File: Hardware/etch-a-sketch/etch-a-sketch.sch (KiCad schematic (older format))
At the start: 37 parts, among them J1 USART, J2 Conn_02x05_Odd_Even, J3 OLED, J4 Micro USB B, SW1 Encoder 1, SW2 Encoder 2, U1 AMS1117-3.3, U2 STM32F401RET6

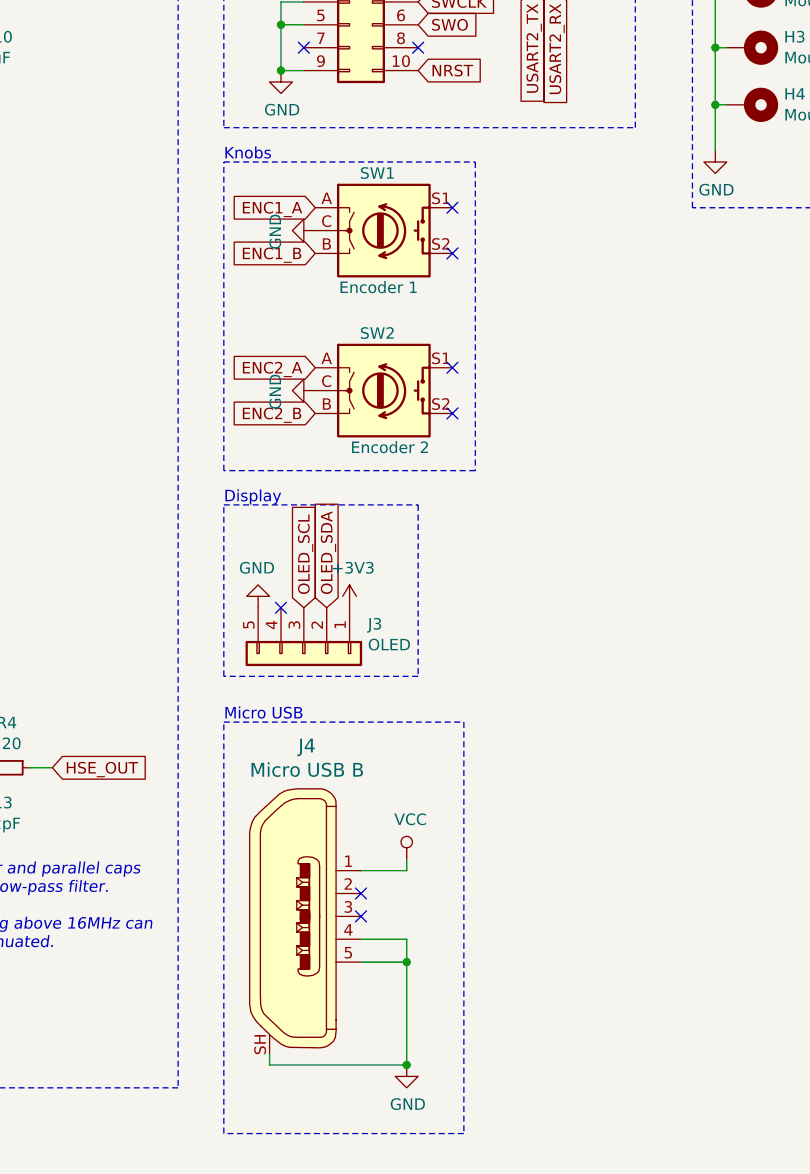
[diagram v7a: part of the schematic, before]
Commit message: feat: connect encoder switches to act as NRST button
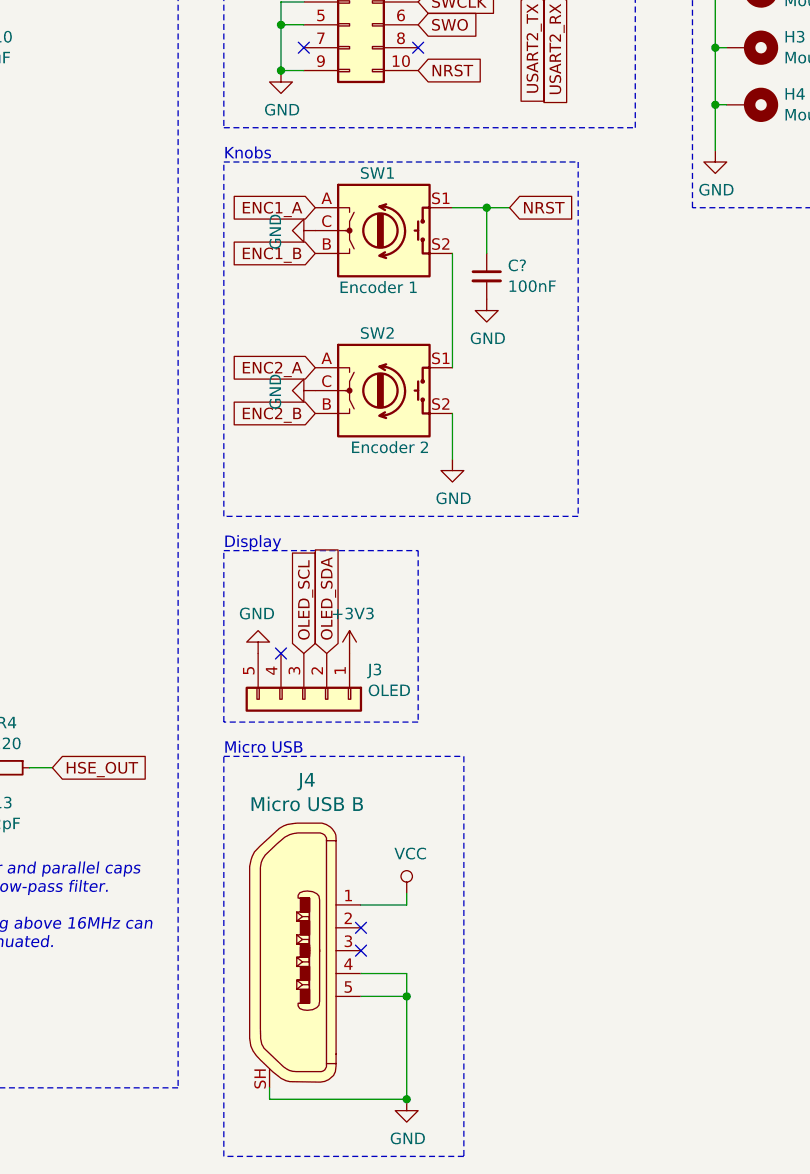
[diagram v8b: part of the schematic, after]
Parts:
- added C?: 100nF, symbol Device:C_Small
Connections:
- net GND: now also SW2.S2, C?.2
- net NRST: now also SW1.S1, C?.1
- net at SW2.S1: now also SW1.S2
- no-connect marks 44 -> 40
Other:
- moved on the sheet: J3, J4
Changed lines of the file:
@@
 NoConn ~ 2850 4300
 NoConn ~ 2850 4200
-NoConn ~ 6400 4450
-NoConn ~ 6400 4250
-NoConn ~ 6400 3750
-NoConn ~ 6400 3550
 $Comp
 L power:GND #PWR013
@@
 L power:GND #PWR019
 U 1 1 5EC0AEF0
-P 5550 5300
-F 0 "#PWR019" H 5550 5050 50  0001 C CNN
-F 1 "GND" H 5555 5127 50  0000 C CNN
-F 2 "" H 5550 5300 50  0001 C CNN
-F 3 "" H 5550 5300 50  0001 C CNN
-	1    5550 5300
+P 5550 5500
+F 0 "#PWR019" H 5550 5250 50  0001 C CNN
+F 1 "GND" H 5555 5327 50  0000 C CNN
+F 2 "" H 5550 5500 50  0001 C CNN
+F 3 "" H 5550 5500 50  0001 C CNN
+	1    5550 5500
 	-1   0    0    1
 $EndComp
-NoConn ~ 5650 5300
-Text GLabel 5850 5300 1    50   Input ~ 0
+NoConn ~ 5650 5500
+Text GLabel 5850 5500 1    50   Input ~ 0
 OLED_SDA
-Text GLabel 5750 5300 1    50   Input ~ 0
+Text GLabel 5750 5500 1    50   Input ~ 0
 OLED_SCL
 $Comp
 L power:+3V3 #PWR020
 U 1 1 5EC0F37C
-P 5950 5300
-F 0 "#PWR020" H 5950 5150 50  0001 C CNN
-F 1 "+3V3" H 5965 5473 50  0000 C CNN
-F 2 "" H 5950 5300 50  0001 C CNN
-F 3 "" H 5950 5300 50  0001 C CNN
-	1    5950 5300
+P 5950 5500
+F 0 "#PWR020" H 5950 5350 50  0001 C CNN
+F 1 "+3V3" H 5965 5673 50  0000 C CNN
+F 2 "" H 5950 5500 50  0001 C CNN
+F 3 "" H 5950 5500 50  0001 C CNN
+	1    5950 5500
 	1    0    0    -1
 $EndComp
@@
 Debug
 Wire Notes Line
-	5400 3350 6500 3350
-Wire Notes Line
-	6500 3350 6500 4700
-Wire Notes Line
-	6500 4700 5400 4700
-Wire Notes Line
-	5400 4700 5400 3350
-Wire Notes Line
-	5400 4850 6250 4850
-Wire Notes Line
-	6250 4850 6250 5600
-Wire Notes Line
-	6250 5600 5400 5600
-Wire Notes Line
-	5400 5600 5400 4850
-Text Notes 5400 4850 0    50   ~ 0
+	5400 3350 6950 3350
+Wire Notes Line
+	6950 3350 6950 4900
+Wire Notes Line
+	6950 4900 5400 4900
+Wire Notes Line
+	5400 4900 5400 3350
+Wire Notes Line
+	5400 5050 6250 5050
+Wire Notes Line
+	6250 5050 6250 5800
+Wire Notes Line
+	6250 5800 5400 5800
+Wire Notes Line
+	5400 5800 5400 5050
+Text Notes 5400 5050 0    50   ~ 0
 Display
 Text Notes 5400 3350 0    50   ~ 0
@@
 L Connector_Generic:Conn_01x05 J3
 U 1 1 5ED42D60
-P 5750 5500
-F 0 "J3" V 5622 5780 50  0000 L CNN
-F 1 "OLED" V 5713 5780 50  0000 L CNN
-F 2 "Connector_PinSocket_2.54mm:PinSocket_1x05_P2.54mm_Vertical" H 5750 5500 50  0001 C CNN
-F 3 "~" H 5750 5500 50  0001 C CNN
-	1    5750 5500
+P 5750 5700
+F 0 "J3" V 5622 5980 50  0000 L CNN
+F 1 "OLED" V 5713 5980 50  0000 L CNN
+F 2 "Connector_PinSocket_2.54mm:PinSocket_1x05_P2.54mm_Vertical" H 5750 5700 50  0001 C CNN
+F 3 "~" H 5750 5700 50  0001 C CNN
+	1    5750 5700
 	0    1    1    0
 $EndComp
@@
 Mounting Holes
 Wire Notes Line
-	5400 5800 6450 5800
-Wire Notes Line
-	6450 5800 6450 7600
-Wire Notes Line
-	6450 7600 5400 7600
-Wire Notes Line
-	5400 7600 5400 5800
-Text Notes 5400 5800 0    50   ~ 0
+	5400 5950 6450 5950
+Wire Notes Line
+	6450 5950 6450 7700
+Wire Notes Line
+	6450 7700 5400 7700
+Wire Notes Line
+	5400 7700 5400 5950
+Text Notes 5400 5950 0    50   ~ 0
 Micro USB
 NoConn ~ 1550 6000
@@
 L dk_USB-DVI-HDMI-Connectors:10118194-0001LF J4
 U 1 1 5EACED3E
-P 5700 6650
-F 0 "J4" H 5764 7395 60  0000 C CNN
-F 1 "Micro USB B" H 5764 7289 60  0000 C CNN
-F 2 "digikey-footprints:USB_Micro_B_Female_10118194-0001LF" H 5900 6850 60  0001 L CNN
-F 3 "http://www.amphenol-icc.com/media/wysiwyg/files/drawing/10118194.pdf" H 5900 6950 60  0001 L CNN
-F 4 "609-4618-1-ND" H 5900 7050 60  0001 L CNN "Digi-Key_PN"
-F 5 "10118194-0001LF" H 5900 7150 60  0001 L CNN "MPN"
-F 6 "Connectors, Interconnects" H 5900 7250 60  0001 L CNN "Category"
-F 7 "USB, DVI, HDMI Connectors" H 5900 7350 60  0001 L CNN "Family"
-F 8 "http://www.amphenol-icc.com/media/wysiwyg/files/drawing/10118194.pdf" H 5900 7450 60  0001 L CNN "DK_Datasheet_Link"
-F 9 "/product-detail/en/amphenol-icc-fci/10118194-0001LF/609-4618-1-ND/2785382" H 5900 7550 60  0001 L CNN "DK_Detail_Page"
-F 10 "CONN RCPT USB2.0 MICRO B SMD R/A" H 5900 7650 60  0001 L CNN "Description"
-F 11 "Amphenol ICC (FCI)" H 5900 7750 60  0001 L CNN "Manufacturer"
-F 12 "Active" H 5900 7850 60  0001 L CNN "Status"
-	1    5700 6650
-	1    0    0    -1
-$EndComp
-NoConn ~ 6000 6550
-NoConn ~ 6000 6650
-Wire Wire Line
-	6000 6450 6200 6450
-Wire Wire Line
-	6200 6450 6200 6400
+P 5700 6800
+F 0 "J4" H 5764 7545 60  0000 C CNN
+F 1 "Micro USB B" H 5764 7439 60  0000 C CNN
+F 2 "digikey-footprints:USB_Micro_B_Female_10118194-0001LF" H 5900 7000 60  0001 L CNN
+F 3 "http://www.amphenol-icc.com/media/wysiwyg/files/drawing/10118194.pdf" H 5900 7100 60  0001 L CNN
+F 4 "609-4618-1-ND" H 5900 7200 60  0001 L CNN "Digi-Key_PN"
+F 5 "10118194-0001LF" H 5900 7300 60  0001 L CNN "MPN"
+F 6 "Connectors, Interconnects" H 5900 7400 60  0001 L CNN "Category"
+F 7 "USB, DVI, HDMI Connectors" H 5900 7500 60  0001 L CNN "Family"
+F 8 "http://www.amphenol-icc.com/media/wysiwyg/files/drawing/10118194.pdf" H 5900 7600 60  0001 L CNN "DK_Datasheet_Link"
+F 9 "/product-detail/en/amphenol-icc-fci/10118194-0001LF/609-4618-1-ND/2785382" H 5900 7700 60  0001 L CNN "DK_Detail_Page"
+F 10 "CONN RCPT USB2.0 MICRO B SMD R/A" H 5900 7800 60  0001 L CNN "Description"
+F 11 "Amphenol ICC (FCI)" H 5900 7900 60  0001 L CNN "Manufacturer"
+F 12 "Active" H 5900 8000 60  0001 L CNN "Status"
+	1    5700 6800
+	1    0    0    -1
+$EndComp
+NoConn ~ 6000 6700
+NoConn ~ 6000 6800
+Wire Wire Line
+	6000 6600 6200 6600
+Wire Wire Line
+	6200 6600 6200 6550
 $Comp
 L power:GND #PWR025
 U 1 1 5EAE82FD
-P 6200 7300
-F 0 "#PWR025" H 6200 7050 50  0001 C CNN
-F 1 "GND" H 6205 7127 50  0000 C CNN
-F 2 "" H 6200 7300 50  0001 C CNN
-F 3 "" H 6200 7300 50  0001 C CNN
-	1    6200 7300
-	1    0    0    -1
-$EndComp
-Wire Wire Line
-	6000 6750 6200 6750
-Wire Wire Line
-	6200 6750 6200 6850
-Wire Wire Line
-	6000 6850 6200 6850
-Connection ~ 6200 6850
-Wire Wire Line
-	6200 6850 6200 7300
-Wire Wire Line
-	5600 7250 5600 7300
-Wire Wire Line
-	5600 7300 6200 7300
-Connection ~ 6200 7300
+P 6200 7450
+F 0 "#PWR025" H 6200 7200 50  0001 C CNN
+F 1 "GND" H 6205 7277 50  0000 C CNN
+F 2 "" H 6200 7450 50  0001 C CNN
+F 3 "" H 6200 7450 50  0001 C CNN
+	1    6200 7450
+	1    0    0    -1
+$EndComp
+Wire Wire Line
+	6000 6900 6200 6900
+Wire Wire Line
+	6200 6900 6200 7000
+Wire Wire Line
+	6000 7000 6200 7000
+Connection ~ 6200 7000
+Wire Wire Line
+	6200 7000 6200 7450
+Wire Wire Line
+	5600 7400 5600 7450
+Wire Wire Line
+	5600 7450 6200 7450
+Connection ~ 6200 7450
 $Comp
 L power:VCC #PWR024
 U 1 1 5EAFBEE0
-P 6200 6400
-F 0 "#PWR024" H 6200 6250 50  0001 C CNN
-F 1 "VCC" H 6217 6573 50  0000 C CNN
-F 2 "" H 6200 6400 50  0001 C CNN
-F 3 "" H 6200 6400 50  0001 C CNN
-	1    6200 6400
-	1    0    0    -1
-$EndComp
+P 6200 6550
+F 0 "#PWR024" H 6200 6400 50  0001 C CNN
+F 1 "VCC" H 6217 6723 50  0000 C CNN
+F 2 "" H 6200 6550 50  0001 C CNN
+F 3 "" H 6200 6550 50  0001 C CNN
+	1    6200 6550
+	1    0    0    -1
+$EndComp
+Text GLabel 6650 3550 2    50   Input ~ 0
+NRST
+$Comp
+L power:GND #PWR?
+U 1 1 5EB42673
+P 6400 4650
+F 0 "#PWR?" H 6400 4400 50  0001 C CNN
+F 1 "GND" H 6405 4477 50  0000 C CNN
+F 2 "" H 6400 4650 50  0001 C CNN
+F 3 "" H 6400 4650 50  0001 C CNN
+	1    6400 4650
+	1    0    0    -1
+$EndComp
+Wire Wire Line
+	6400 3750 6400 4250
+$Comp
+L Device:C_Small C?
+U 1 1 5EB51000
+P 6550 3850
+F 0 "C?" H 6642 3896 50  0000 L CNN
+F 1 "100nF" H 6642 3805 50  0000 L CNN
+F 2 "" H 6550 3850 50  0001 C CNN
+F 3 "~" H 6550 3850 50  0001 C CNN
+	1    6550 3850
+	1    0    0    -1
+$EndComp
+$Comp
+L power:GND #PWR?
+U 1 1 5EB7A007
+P 6550 3950
+F 0 "#PWR?" H 6550 3700 50  0001 C CNN
+F 1 "GND" H 6555 3777 50  0000 C CNN
+F 2 "" H 6550 3950 50  0001 C CNN
+F 3 "" H 6550 3950 50  0001 C CNN
+	1    6550 3950
+	1    0    0    -1
+$EndComp
+Wire Wire Line
+	6400 3550 6550 3550
+Wire Wire Line
+	6550 3550 6550 3750
+Connection ~ 6550 3550
+Wire Wire Line
+	6550 3550 6650 3550
+Wire Wire Line
+	6400 4450 6400 4650
 $EndSCHEMATC
